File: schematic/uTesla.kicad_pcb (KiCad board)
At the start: 2 copper layers, 140 x 140 mm, 74 parts, among them J1 DC-005, J2 Flash, J3 IO, J4 MSD-1-A, Q1 IRFZ44N, Q2 IRFZ44N, Q3 IRFZ44N, SW1 RST, T1 1:1, U1 MP9486A, U2 AMS1117-3.3, U3 ATmega328P-A, Y1 HC-49 16MHz

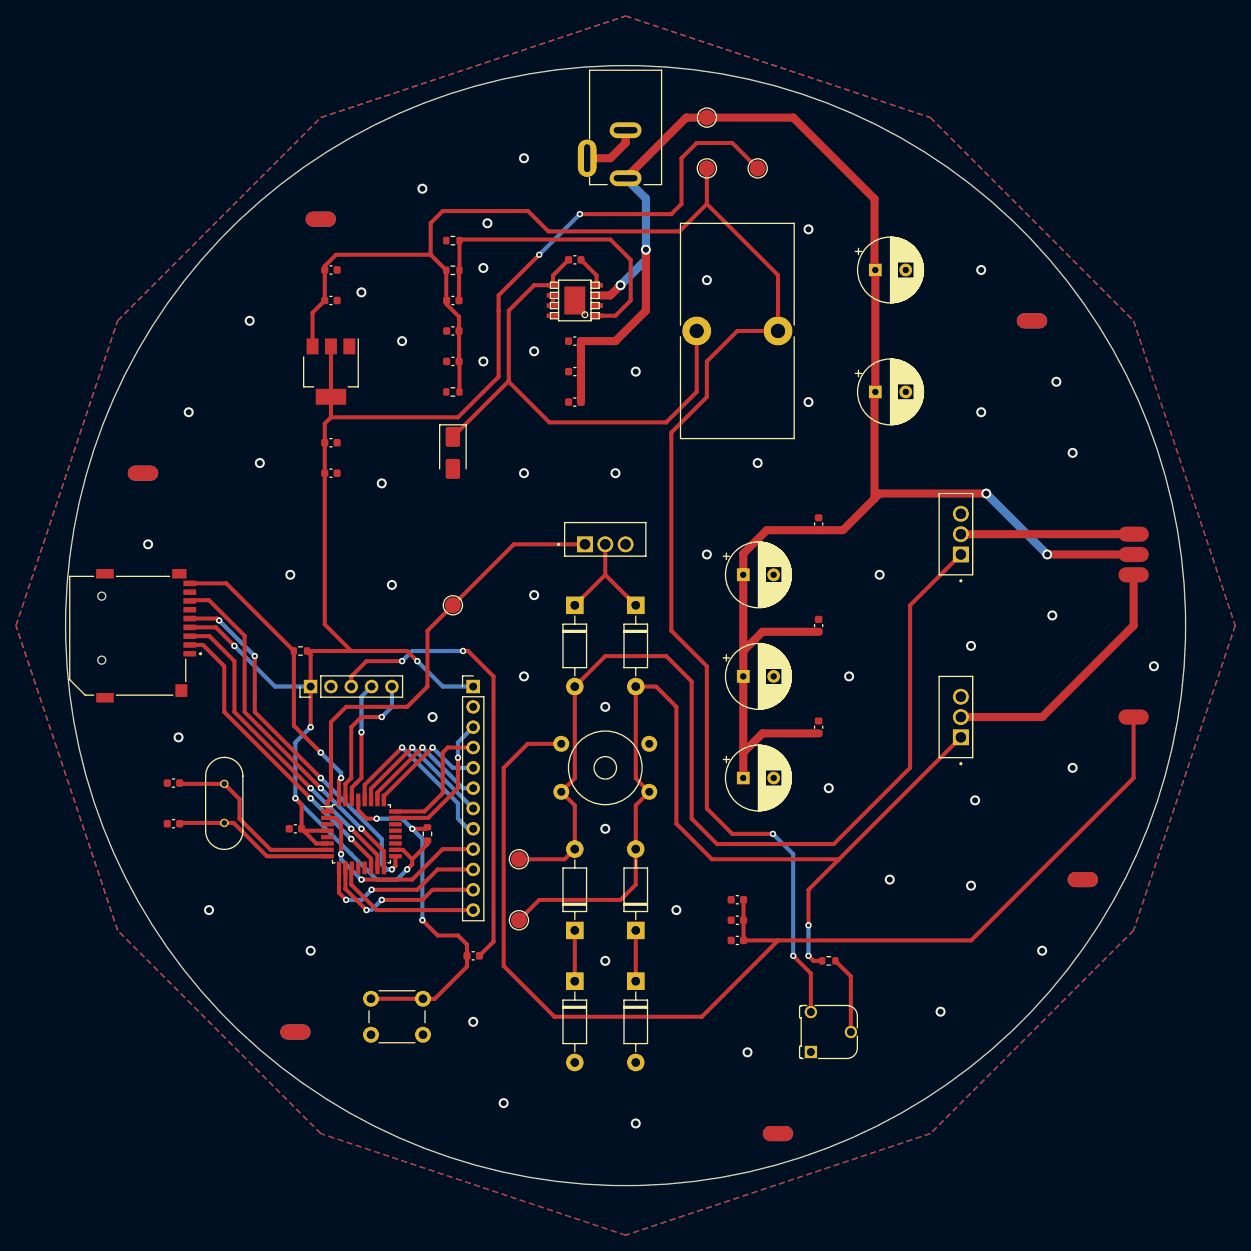
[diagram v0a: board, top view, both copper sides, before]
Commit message: Add silkscreen labels
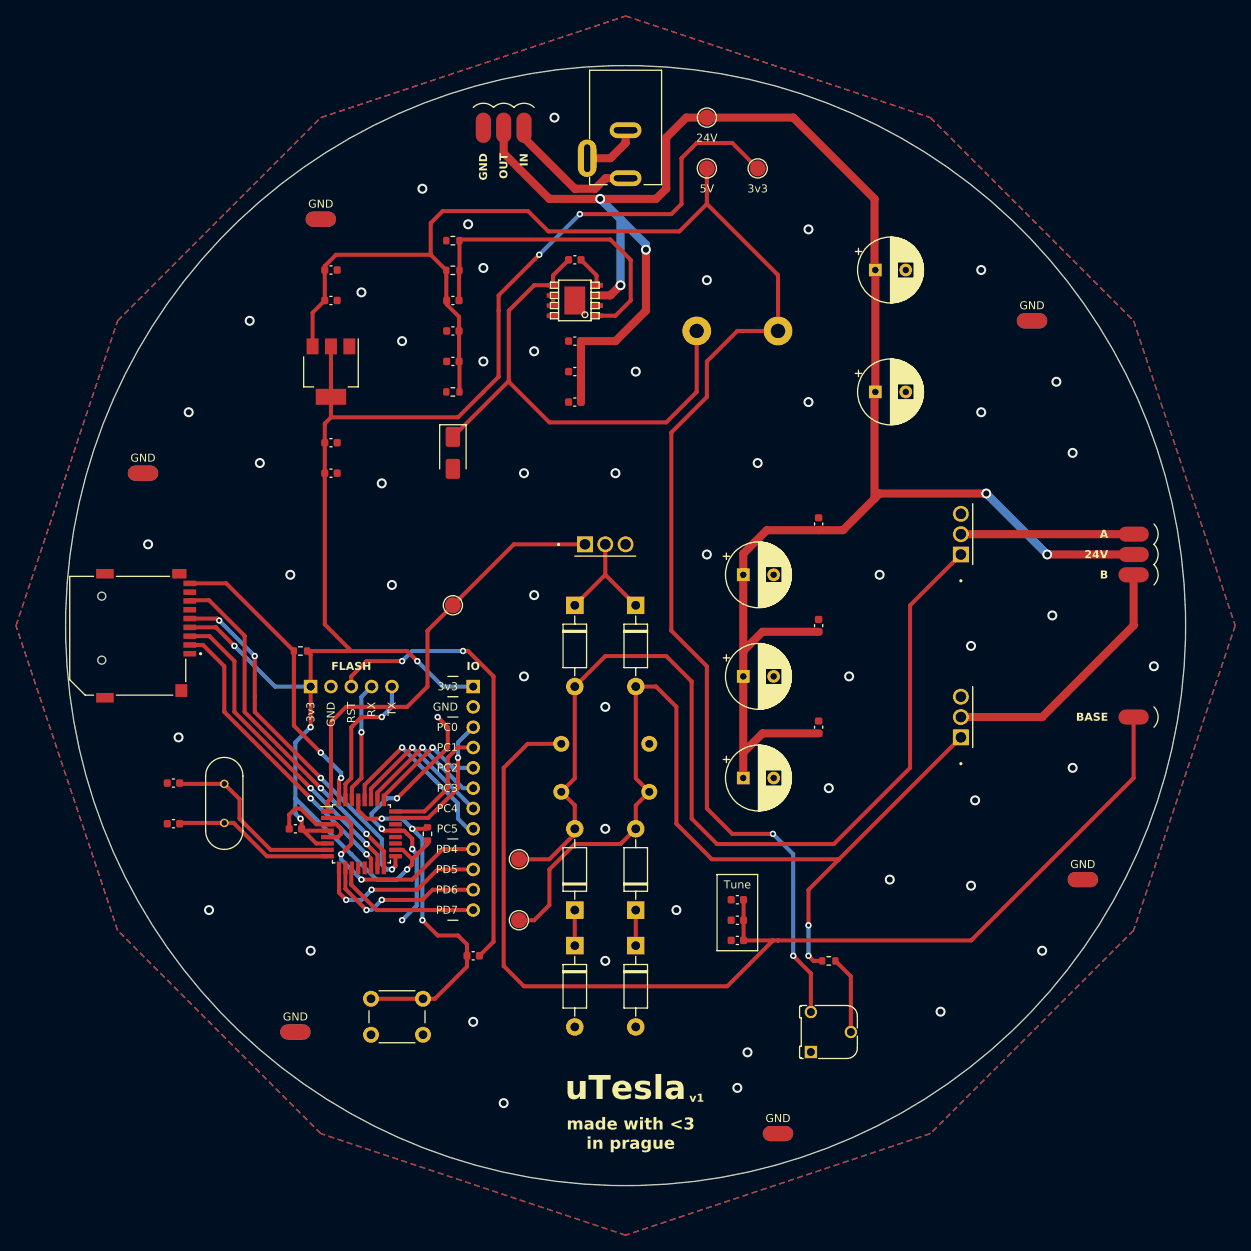
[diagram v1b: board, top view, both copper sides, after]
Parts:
- added J19: ~, Custom:SolderPad-3pin, F.Cu at (137.2, 26.7)
- moved D6 4.44 mm to (146.1, 128.9)
- moved D7 4.44 mm to (153.7, 128.9)
- moved D4 2.54 mm to (146.1, 124.5)
- moved D5 2.54 mm to (153.7, 124.5)
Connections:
- J1 pad 4: +24V -> Net-(J1-Pad4)
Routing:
- net GND: track 7.18 -> 54.5 mm, vias 53 -> 57
- net +24V: track 224.2 -> 251.0 mm, vias 4 -> 5
- net Net-(J1-Pad4): track 0.00 -> 17.1 mm
- net /Contacts/Base: track 144.0 -> 140.2 mm
- net Net-(D5-K): track 6.35 -> 4.45 mm
- net Net-(D4-K): track 6.35 -> 4.45 mm
- net Net-(J3-Pin_9): track 25.6 -> 27.4 mm
- net Net-(D3-A): track 122.7 -> 121.2 mm
- net Net-(D2-A): track 125.7 -> 124.6 mm
- net Net-(J3-Pin_4): track 16.0 -> 15.3 mm
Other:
- board text added: "24V"
- board text added: "3v3"
- board text added: "5V"
- board text added: "A"
- board text added: "B"
- board text added: "BASE"
- board text added: "FLASH"
- board text added: "GND"
- board text added: "IN"
- board text added: "IO"
- board text added: "OUT"
- board text added: "PC0"
- board text added: "PC1"
- board text added: "PC2"
- board text added: "PC3"
- board text added: "PC4"
- board text added: "PC5"
- board text added: "PD4"
- board text added: "PD5"
- board text added: "PD6"
- board text added: "PD7"
- board text added: "RST"
- board text added: "RX"
- board text added: "TX"
- board text added: "Tune"
- board text added: "made with <3 in prague"
- board text added: "uTesla"
- board text added: "v1"
